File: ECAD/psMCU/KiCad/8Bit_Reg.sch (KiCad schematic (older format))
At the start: 6 parts, among them U185 SN74LVC1G04DCK, U186 CD74HC173PW, U187 CD74HC173PW

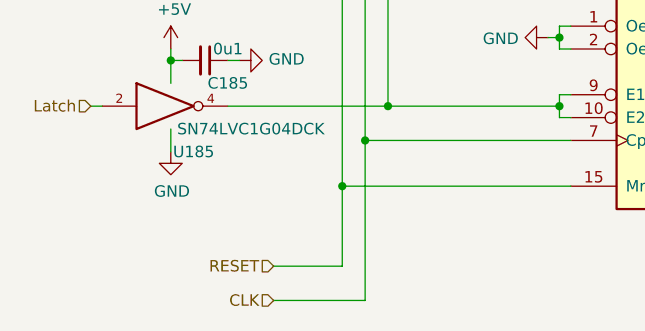
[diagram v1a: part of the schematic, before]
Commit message: Sch: Improved Clk/Reset distribution, moved to global labels
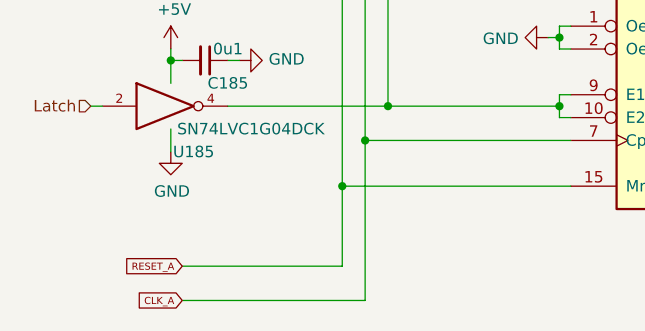
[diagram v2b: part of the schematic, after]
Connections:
- net CLK renamed CLK_A
- net RESET renamed RESET_A
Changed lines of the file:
@@
 $Descr A4 11693 8268
 encoding utf-8
-Sheet 89 96
+Sheet 84 97
 Title "psMCU"
 Date "2022-02-13"
@@
 Wire Wire Line
 	4150 4350 4900 4350
-Text HLabel 3650 5200 0    50   Input ~ 0
-CLK
-Text HLabel 3650 5050 0    50   Input ~ 0
-RESET
 Wire Wire Line
 	3950 4700 4950 4700
 Wire Wire Line
 	3950 4700 3950 5050
-Wire Wire Line
-	3650 5050 3950 5050
 Connection ~ 3950 4700
 Wire Wire Line
 	4050 5200 4050 4500
-Wire Wire Line
-	3650 5200 4050 5200
 Connection ~ 4050 4500
+Text GLabel 3250 5200 0    31   Input ~ 0
+CLK_A
+Text GLabel 3250 5050 0    31   Input ~ 0
+RESET_A
+Wire Wire Line
+	3250 5200 4050 5200
+Wire Wire Line
+	3250 5050 3950 5050
 Wire Bus Line
 	6550 900  6550 3900

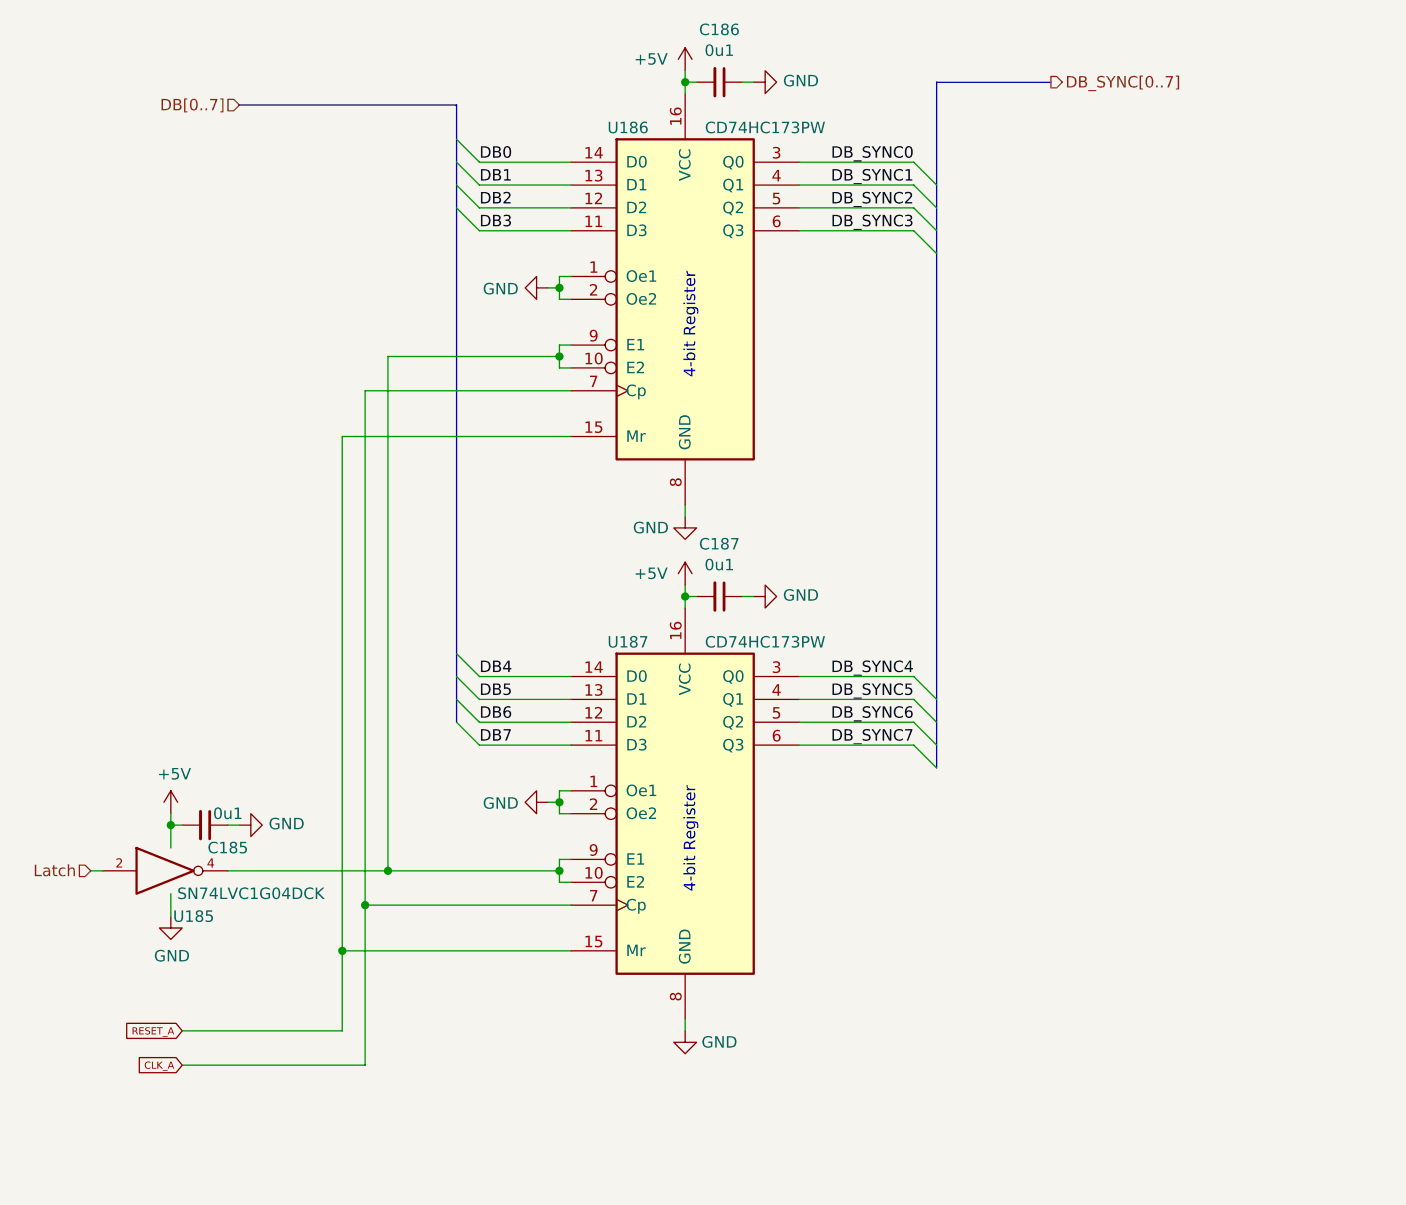
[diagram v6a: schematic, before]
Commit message: Sch: More cleanup, fixed page descriptions.
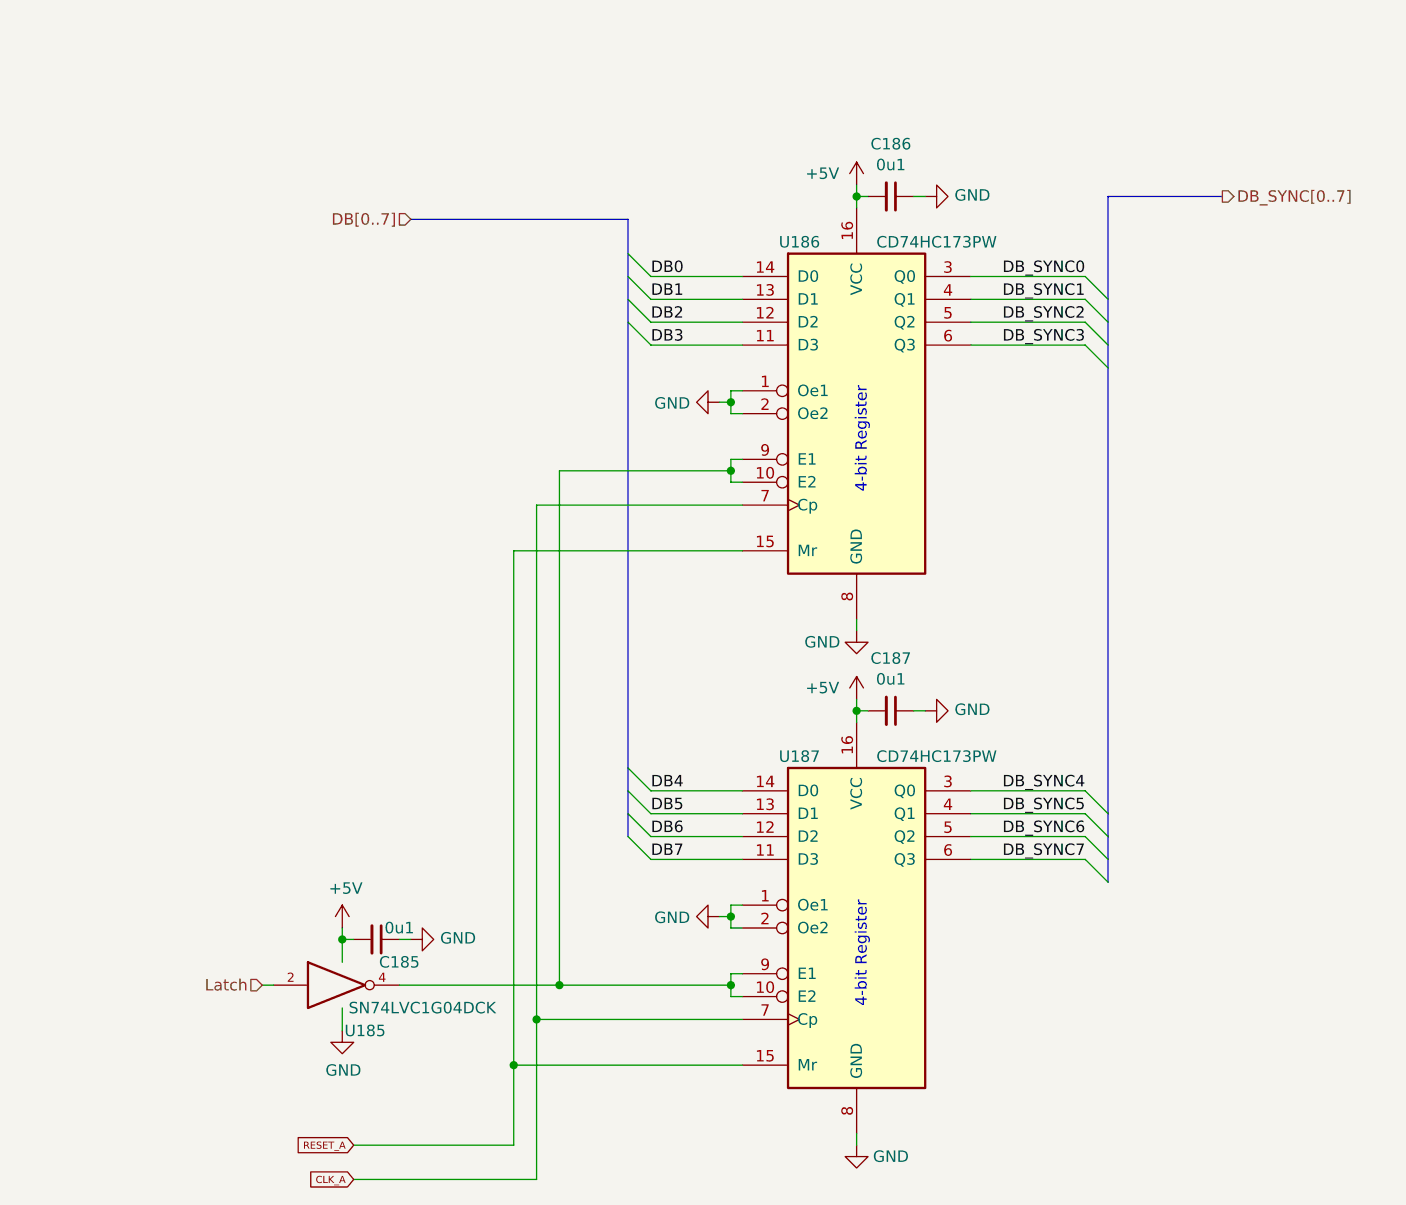
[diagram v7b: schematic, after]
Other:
- moved on the sheet: C185, C186, C187, U185, U186, U187
